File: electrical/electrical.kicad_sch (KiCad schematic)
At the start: 0 parts

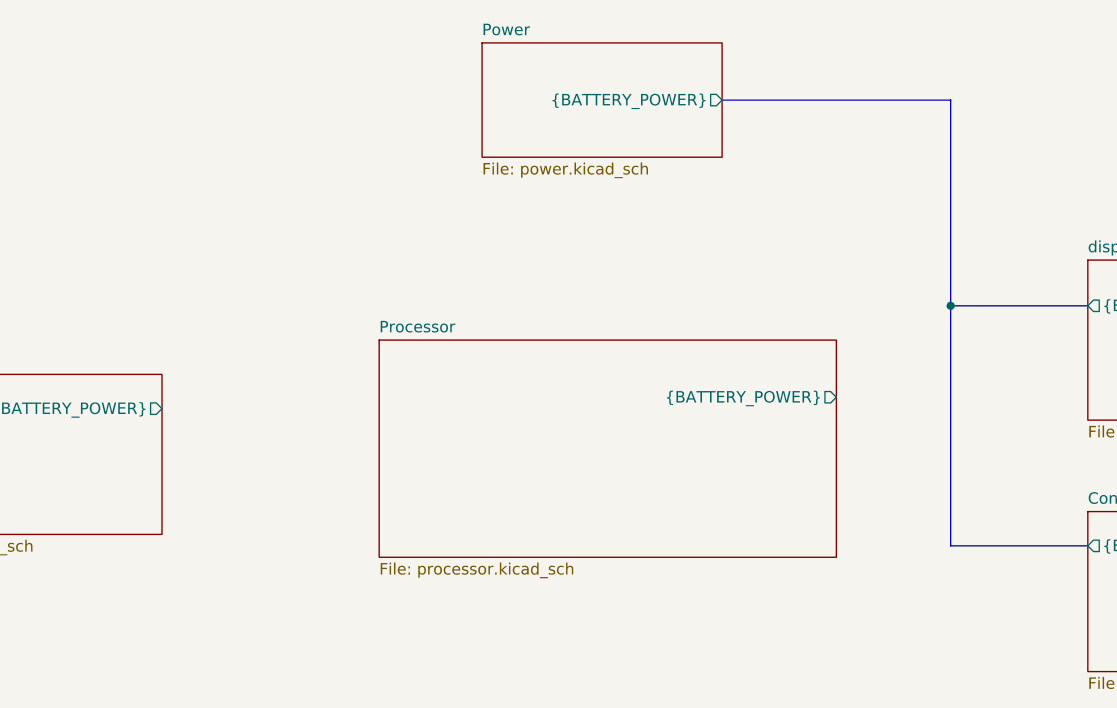
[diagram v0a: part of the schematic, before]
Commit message: #3 Implementing base schematic for processor.
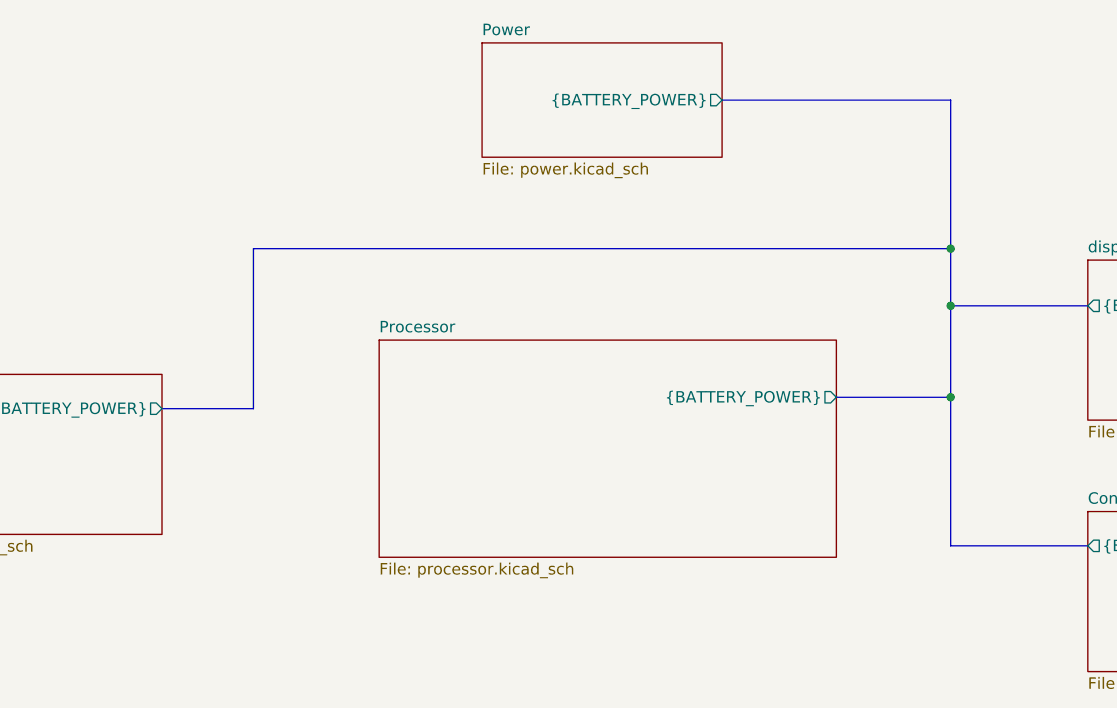
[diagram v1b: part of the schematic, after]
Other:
- title: Etchasketch System Layout -> Etchasketch - System Diagram
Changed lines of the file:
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@@
 	(paper "A4")
 	(title_block
-		(title "Etchasketch System Layout")
+		(title "Etchasketch - System Diagram")
 		(rev "1")
 		(company "Alumapower")
@@
 		(color 0 0 0 0)
 	)
+	(junction
+		(at 179.07 74.93)
+		(diameter 0)
+		(color 0 0 0 0)
+	)
+	(junction
+		(at 179.07 91.44)
+		(diameter 0)
+		(color 0 0 0 0)
+	)
 	(bus
 		(pts
-			(xy 179.07 58.42) (xy 179.07 81.28)
+			(xy 179.07 74.93) (xy 179.07 81.28)
+		)
+		(stroke
+			(width 0)
+			(type default)
+		)
+	)
+	(bus
+		(pts
+			(xy 179.07 58.42) (xy 179.07 74.93)
+		)
+		(stroke
+			(width 0)
+			(type default)
+		)
+	)
+	(bus
+		(pts
+			(xy 166.37 91.44) (xy 179.07 91.44)
+		)
+		(stroke
+			(width 0)
+			(type default)
+		)
+	)
+	(bus
+		(pts
+			(xy 101.6 74.93) (xy 101.6 92.71)
 		)
 		(stroke
@@
 	(bus
 		(pts
-			(xy 179.07 81.28) (xy 179.07 107.95)
+			(xy 179.07 81.28) (xy 179.07 91.44)
 		)
 		(stroke
@@
 		)
 		(stroke
+			(width 0)
+			(type default)
+		)
+	)
+	(bus
+		(pts
+			(xy 179.07 91.44) (xy 179.07 107.95)
+		)
+		(stroke
+			(width 0)
+			(type default)
+		)
+	)
+	(bus
+		(pts
+			(xy 101.6 92.71) (xy 91.44 92.71)
+		)
+		(stroke
+			(width 0)
+			(type default)
+		)
+	)
+	(bus
+		(pts
+			(xy 179.07 74.93) (xy 101.6 74.93)
+		)
+		(stroke

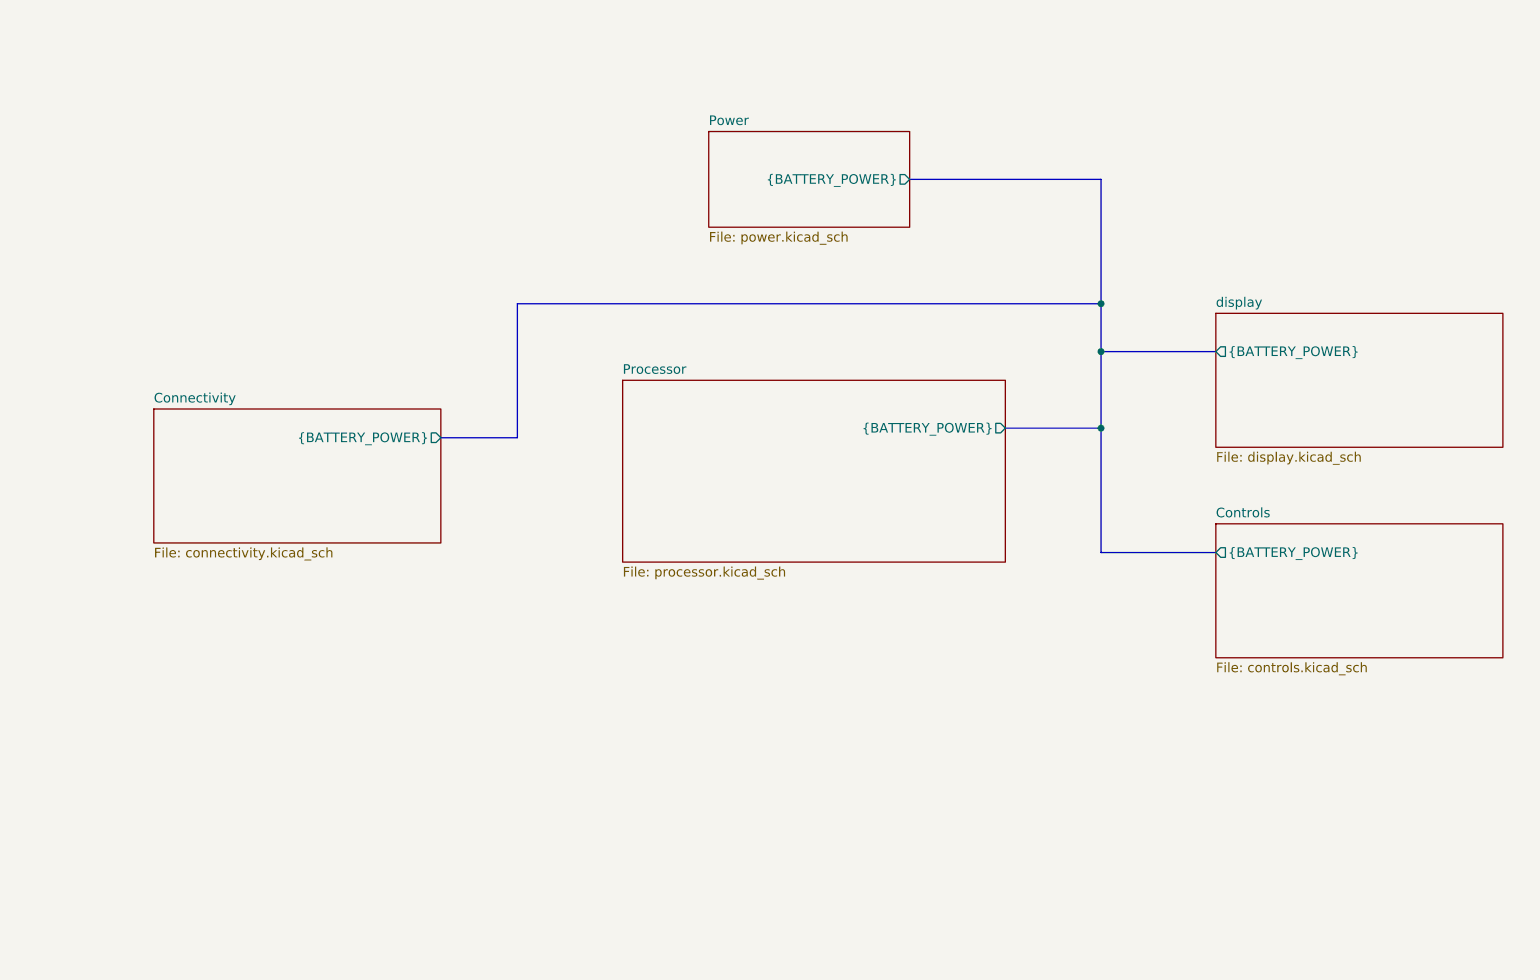
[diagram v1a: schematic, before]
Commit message: #3 Implementing potentionometers and  beginning IOC file creation.
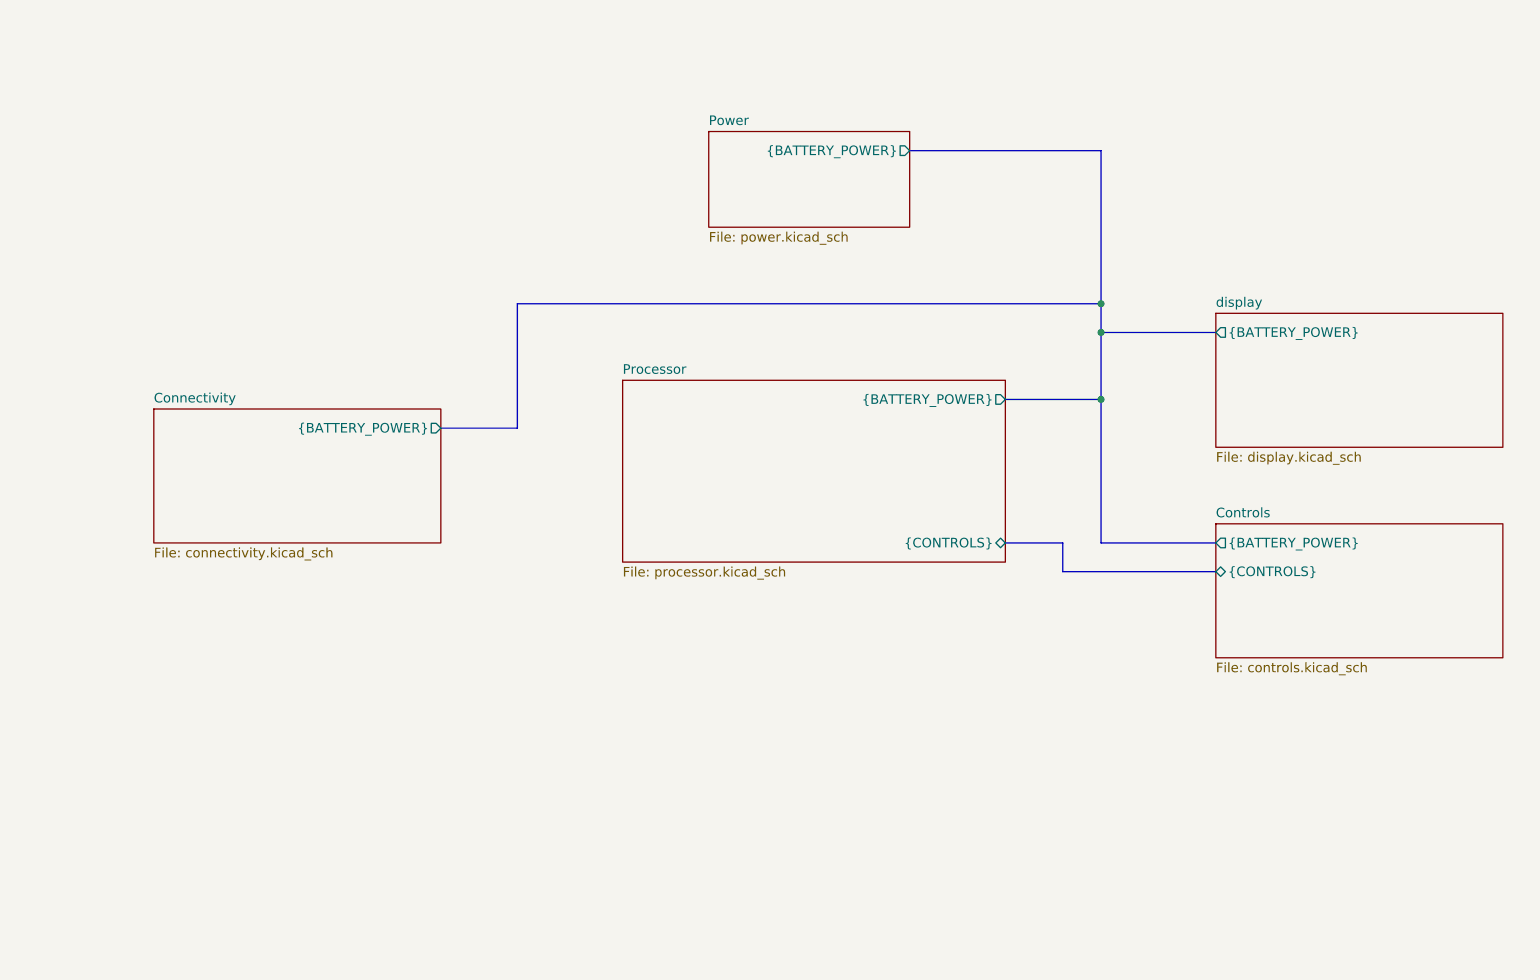
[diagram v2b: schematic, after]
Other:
- sheet Controls ports: added {CONTROLS}; removed none
- sheet Processor ports: added {CONTROLS}; removed none
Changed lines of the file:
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@@
 	)
 	(junction
-		(at 179.07 81.28)
+		(at 179.07 78.74)
 		(diameter 0)
 		(color 0 0 0 0)
@@
 	)
 	(junction
-		(at 179.07 91.44)
+		(at 179.07 87.63)
 		(diameter 0)
 		(color 0 0 0 0)
@@
 	(bus
 		(pts
-			(xy 179.07 74.93) (xy 179.07 81.28)
-		)
-		(stroke
-			(width 0)
-			(type default)
-		)
-	)
-	(bus
-		(pts
-			(xy 179.07 58.42) (xy 179.07 74.93)
-		)
-		(stroke
-			(width 0)
-			(type default)
-		)
-	)
-	(bus
-		(pts
-			(xy 166.37 91.44) (xy 179.07 91.44)
-		)
-		(stroke
-			(width 0)
-			(type default)
-		)
-	)
-	(bus
-		(pts
-			(xy 101.6 74.93) (xy 101.6 92.71)
-		)
-		(stroke
-			(width 0)
-			(type default)
-		)
-	)
-	(bus
-		(pts
-			(xy 179.07 107.95) (xy 194.31 107.95)
-		)
-		(stroke
-			(width 0)
-			(type default)
-		)
-	)
-	(bus
-		(pts
-			(xy 179.07 81.28) (xy 179.07 91.44)
-		)
-		(stroke
-			(width 0)
-			(type default)
-		)
-	)
-	(bus
-		(pts
-			(xy 179.07 81.28) (xy 194.31 81.28)
-		)
-		(stroke
-			(width 0)
-			(type default)
-		)
-	)
-	(bus
-		(pts
-			(xy 179.07 91.44) (xy 179.07 107.95)
-		)
-		(stroke
-			(width 0)
-			(type default)
-		)
-	)
-	(bus
-		(pts
-			(xy 101.6 92.71) (xy 91.44 92.71)
+			(xy 166.37 106.68) (xy 173.99 106.68)
+		)
+		(stroke
+			(width 0)
+			(type default)
+		)
+	)
+	(bus
+		(pts
+			(xy 179.07 74.93) (xy 179.07 78.74)
+		)
+		(stroke
+			(width 0)
+			(type default)
+		)
+	)
+	(bus
+		(pts
+			(xy 179.07 54.61) (xy 179.07 74.93)
+		)
+		(stroke
+			(width 0)
+			(type default)
+		)
+	)
+	(bus
+		(pts
+			(xy 166.37 87.63) (xy 179.07 87.63)
+		)
+		(stroke
+			(width 0)
+			(type default)
+		)
+	)
+	(bus
+		(pts
+			(xy 179.07 78.74) (xy 179.07 87.63)
+		)
+		(stroke
+			(width 0)
+			(type default)
+		)
+	)
+	(bus
+		(pts
+			(xy 101.6 74.93) (xy 101.6 91.44)
+		)
+		(stroke
+			(width 0)
+			(type default)
+		)
+	)
+	(bus
+		(pts
+			(xy 179.07 106.68) (xy 194.31 106.68)
+		)
+		(stroke
+			(width 0)
+			(type default)
+		)
+	)
+	(bus
+		(pts
+			(xy 179.07 78.74) (xy 194.31 78.74)
+		)
+		(stroke
+			(width 0)
+			(type default)
+		)
+	)
+	(bus
+		(pts
+			(xy 101.6 91.44) (xy 91.44 91.44)
 		)
 		(stroke
@@
 	(bus
 		(pts
-			(xy 153.67 58.42) (xy 179.07 58.42)
+			(xy 153.67 54.61) (xy 179.07 54.61)
+		)
+		(stroke
+			(width 0)
+			(type default)
+		)
+	)
+	(bus
+		(pts
+			(xy 173.99 110.49) (xy 194.31 110.49)
+		)
+		(stroke
+			(width 0)
+			(type default)
+		)
+	)
+	(bus
+		(pts
+			(xy 179.07 87.63) (xy 179.07 106.68)
+		)
+		(stroke
+			(width 0)
+			(type default)
+		)
+	)
+	(bus
+		(pts
+			(xy 173.99 106.68) (xy 173.99 110.49)
 		)
 		(stroke
@@
 		)
 		(pin "{BATTERY_POWER}" output
-			(at 166.37 91.44 0)
+			(at 166.37 87.63 0)
+			(effects
+				(font
+					(size 1.27 1.27)
+				)
+				(justify right)
+			)
+		)
+		(pin "{CONTROLS}" bidirectional
+			(at 166.37 106.68 0)
 			(effects
 				(font
@@
 		)
 		(pin "{BATTERY_POWER}" output
-			(at 194.31 81.28 180)
+			(at 194.31 78.74 180)
 			(effects
 				(font
@@
 		)
 		(pin "{BATTERY_POWER}" output
-			(at 194.31 107.95 180)
+			(at 194.31 106.68 180)
+			(effects
+				(font
+					(size 1.27 1.27)
+				)
+				(justify left)
+			)
+		)
+		(pin "{CONTROLS}" bidirectional
+			(at 194.31 110.49 180)
 			(effects
 				(font
@@
 		)
 		(pin "{BATTERY_POWER}" output
-			(at 91.44 92.71 0)
+			(at 91.44 91.44 0)
 			(effects
 				(font
@@
 		)
 		(pin "{BATTERY_POWER}" output
-			(at 153.67 58.42 0)
-			(effects
-				(font
+			(at 153.67 54.61 0)
+			(effects
+				(font

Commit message: #3 Adding controls connections to STM32, updating IOC file to match.
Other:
- company: Alumapower -> AlumaPower
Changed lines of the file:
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@@
 		(title "Etchasketch - System Diagram")
 		(rev "1")
-		(company "Alumapower")
+		(company "AlumaPower")
 	)
 	(junction

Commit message: #3 Updating schematic.
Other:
- sheet display renamed Display
- sheet Connectivity ports: added {CONNECTIVITY}; removed none
- sheet Display ports: added {SCREEN_INTERFACE}; removed none
- sheet Processor ports: added {CONNECTIVITY}, {SCREEN_INTERFACE}; removed none
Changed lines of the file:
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@@
+	(bus
+		(pts
+			(xy 101.6 104.14) (xy 101.6 106.68)
+		)
+		(stroke
+			(width 0)
+			(type default)
+		)
+	)
 	(bus
 		(pts
@@
 	(bus
 		(pts
+			(xy 101.6 106.68) (xy 115.57 106.68)
+		)
+		(stroke
+			(width 0)
+			(type default)
+		)
+	)
+	(bus
+		(pts
 			(xy 179.07 74.93) (xy 179.07 78.74)
 		)
@@
 	(bus
 		(pts
+			(xy 186.69 91.44) (xy 186.69 96.52)
+		)
+		(stroke
+			(width 0)
+			(type default)
+		)
+	)
+	(bus
+		(pts
 			(xy 179.07 78.74) (xy 194.31 78.74)
 		)
@@
 	(bus
 		(pts
+			(xy 91.44 104.14) (xy 101.6 104.14)
+		)
+		(stroke
+			(width 0)
+			(type default)
+		)
+	)
+	(bus
+		(pts
+			(xy 186.69 96.52) (xy 166.37 96.52)
+		)
+		(stroke
+			(width 0)
+			(type default)
+		)
+	)
+	(bus
+		(pts
 			(xy 101.6 91.44) (xy 91.44 91.44)
 		)
@@
 		(pts
 			(xy 173.99 110.49) (xy 194.31 110.49)
+		)
+		(stroke
+			(width 0)
+			(type default)
+		)
+	)
+	(bus
+		(pts
+			(xy 194.31 91.44) (xy 186.69 91.44)
 		)
 		(stroke
@@
 			)
 		)
-		(pin "{BATTERY_POWER}" output
+		(pin "{BATTERY_POWER}" passive
 			(at 166.37 87.63 0)
 			(effects
@@
 			)
 		)
-		(pin "{CONTROLS}" bidirectional
+		(pin "{CONTROLS}" passive
 			(at 166.37 106.68 0)
+			(effects
+				(font
+					(size 1.27 1.27)
+				)
+				(justify right)
+			)
+		)
+		(pin "{CONNECTIVITY}" passive
+			(at 115.57 106.68 180)
+			(effects
+				(font
+					(size 1.27 1.27)
+				)
+				(justify left)
+			)
+		)
+		(pin "{SCREEN_INTERFACE}" passive
+			(at 166.37 96.52 0)
 			(effects
 				(font
@@
 			(color 255 255 194 1.0000)
 		)
-		(property "Sheetname" "display"
+		(property "Sheetname" "Display"
 			(at 194.31 75.4884 0)
 			(effects
@@
 			)
 		)
-		(pin "{BATTERY_POWER}" output
+		(pin "{BATTERY_POWER}" passive
 			(at 194.31 78.74 180)
+			(effects
+				(font
+					(size 1.27 1.27)
+				)
+				(justify left)
+			)
+		)
+		(pin "{SCREEN_INTERFACE}" passive
+			(at 194.31 91.44 180)
 			(effects
 				(font
@@
 			)
 		)
-		(pin "{BATTERY_POWER}" output
+		(pin "{BATTERY_POWER}" passive
 			(at 194.31 106.68 180)
 			(effects
@@
 			)
 		)
-		(pin "{CONTROLS}" bidirectional
+		(pin "{CONTROLS}" passive
 			(at 194.31 110.49 180)
 			(effects
@@
 			)
 		)
-		(pin "{BATTERY_POWER}" output
+		(pin "{BATTERY_POWER}" passive
 			(at 91.44 91.44 0)
+			(effects
+				(font
+					(size 1.27 1.27)
+				)
+				(justify right)
+			)
+		)
+		(pin "{CONNECTIVITY}" passive
+			(at 91.44 104.14 0)
 			(effects
 				(font
@@
 			)
 		)
-		(pin "{BATTERY_POWER}" output
+		(pin "{BATTERY_POWER}" passive
 			(at 153.67 54.61 0)
 			(effects

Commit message: not in working state yet.
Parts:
- added H1, H2, H3, H4: MountingHole, MountingHole:MountingHole_2.2mm_M2, symbol Mechanical:MountingHole

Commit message: #17 Making layout. Errors rpesent.
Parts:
- added H5, H6: MountingHole, MountingHole:MountingHole_2.2mm_M2, symbol Mechanical:MountingHole
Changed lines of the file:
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@@
+	(symbol
+		(lib_id "Mechanical:MountingHole")
+		(at 36.83 153.67 0)
+		(unit 1)
+		(exclude_from_sim no)
+		(in_bom no)
+		(on_board yes)
+		(dnp no)
+		(fields_autoplaced yes)
+		(property "Reference" "H5"
+			(at 39.37 152.3999 0)
+			(effects
+				(font
+					(size 1.27 1.27)
+				)
+				(justify left)
+			)
+		)
+		(property "Value" "MountingHole"
+			(at 39.37 154.9399 0)
+			(effects
+				(font
+					(size 1.27 1.27)
+				)
+				(justify left)
+			)
+		)
+		(property "Footprint" "MountingHole:MountingHole_2.2mm_M2"
+			(at 36.83 153.67 0)
+			(effects
+				(font
+					(size 1.27 1.27)
+				)
+				(hide yes)
+			)
+		)
+		(property "Datasheet" "~"
+			(at 36.83 153.67 0)
+			(effects
+				(font
+					(size 1.27 1.27)
+				)
+				(hide yes)
+			)
+		)
+		(property "Description" "Mounting Hole without connection"
+			(at 36.83 153.67 0)
+			(effects
+				(font
+					(size 1.27 1.27)
+				)
+				(hide yes)
+			)
+		)
+		(instances
+			(project "electrical"
+				(path "/0ea7de92-e138-4a6c-b193-fca6869c3a12"
+					(reference "H5")
+					(unit 1)
+				)
+			)
+		)
+	)
 	(symbol
 		(lib_id "Mechanical:MountingHole")
@@
 		)
 	)
+	(symbol
+		(lib_id "Mechanical:MountingHole")
+		(at 36.83 160.02 0)
+		(unit 1)
+		(exclude_from_sim no)
+		(in_bom no)
+		(on_board yes)
+		(dnp no)
+		(fields_autoplaced yes)
+		(property "Reference" "H6"
+			(at 39.37 158.7499 0)
+			(effects
+				(font
+					(size 1.27 1.27)
+				)
+				(justify left)
+			)
+		)
+		(property "Value" "MountingHole"
+			(at 39.37 161.2899 0)
+			(effects
+				(font
+					(size 1.27 1.27)
+				)
+				(justify left)
+			)
+		)
+		(property "Footprint" "MountingHole:MountingHole_2.2mm_M2"
+			(at 36.83 160.02 0)
+			(effects
+				(font
+					(size 1.27 1.27)
+				)
+				(hide yes)
+			)
+		)
+		(property "Datasheet" "~"
+			(at 36.83 160.02 0)
+			(effects
+				(font
+					(size 1.27 1.27)
+				)
+				(hide yes)
+			)
+		)
+		(property "Description" "Mounting Hole without connection"
+			(at 36.83 160.02 0)
+			(effects
+				(font
+					(size 1.27 1.27)
+				)
+				(hide yes)
+			)
+		)
+		(instances
+			(project "electrical"
+				(path "/0ea7de92-e138-4a6c-b193-fca6869c3a12"
+					(reference "H6")
+					(unit 1)
+				)
+			)
+		)
+	)
 	(sheet
 		(at 115.57 85.09)
@@
 			)
 		)
-		(pin "{BATTERY_POWER}" passive
+		(pin "{BATTERY_POWER}" output
 			(at 91.44 91.44 0)
 			(effects

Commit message: Making progress on schematic and developing IOC.
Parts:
- removed H1, H2, H3, H4, H5, H6: MountingHole, MountingHole:MountingHole_2.2mm_M2, symbol Mechanical:MountingHole
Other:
- removed sheet Connectivity
- removed sheet Controls
- removed sheet Display
- added sheet Accelerometer (accelerometer.kicad_sch)
- added sheet Screen (screen.kicad_sch)
- added sheet User Input (user_input.kicad_sch)
- added sheet WiFi (wifi.kicad_sch)
- sheet Power ports: added none; removed {BATTERY_POWER}
- sheet Processor ports: added {WIFI_INTERFACE}; removed {BATTERY_POWER}, {CONNECTIVITY}, {CONTROLS}, {SCREEN_INTERFACE}
- company: AlumaPower -> (none)
- title: Etchasketch - System Diagram -> (none)

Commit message: Adding user input.
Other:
- sheet Processor ports: added {USER_INPUTS}; removed none
- sheet User Input ports: added {USER_INPUTS}; removed none
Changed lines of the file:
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@@
+		)
+	)
+	(bus
+		(pts
+			(xy 125.73 86.36) (xy 125.73 64.77)
+		)
+		(stroke
+			(width 0)
+			(type default)
+		)
+	)
+	(bus
+		(pts
+			(xy 116.84 86.36) (xy 125.73 86.36)
+		)
+		(stroke
+			(width 0)
+			(type default)
+		)
+	)
+	(bus
+		(pts
+			(xy 125.73 64.77) (xy 117.15 64.77)
+		)
+		(stroke
+			(width 0)
+			(type default)
 		)
 	)
@@
 			)
 		)
+		(pin "{USER_INPUTS}" passive
+			(at 117.15 64.77 0)
+			(effects
+				(font
+					(size 1.27 1.27)
+				)
+				(justify right)
+			)
+		)
 		(instances
 			(project "electrical"
@@
 			)
 		)
+		(pin "{USER_INPUTS}" passive
+			(at 117.15 86.36 0)
+			(effects
+				(font
+					(size 1.27 1.27)
+				)
+				(justify right)
+			)
+		)
